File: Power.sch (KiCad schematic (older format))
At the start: 15 parts, among them U301 AOZ6605PI-1

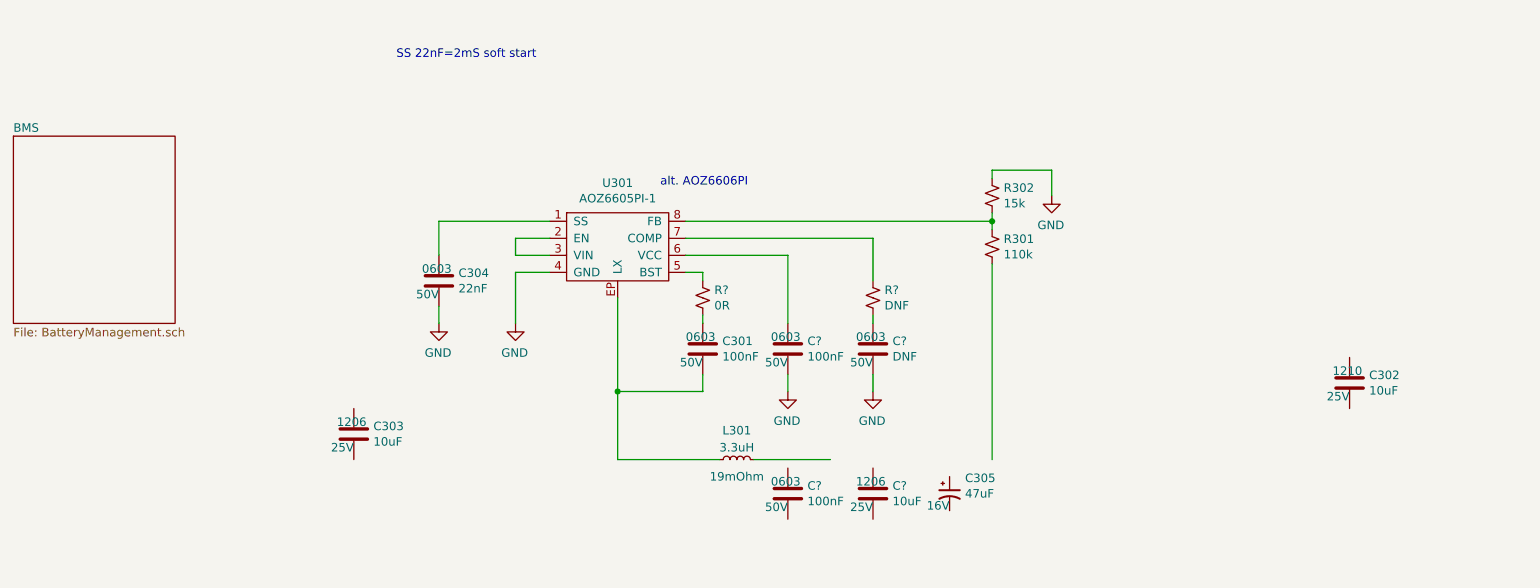
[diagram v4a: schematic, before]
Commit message: Changing structure, RM old power circuitry.
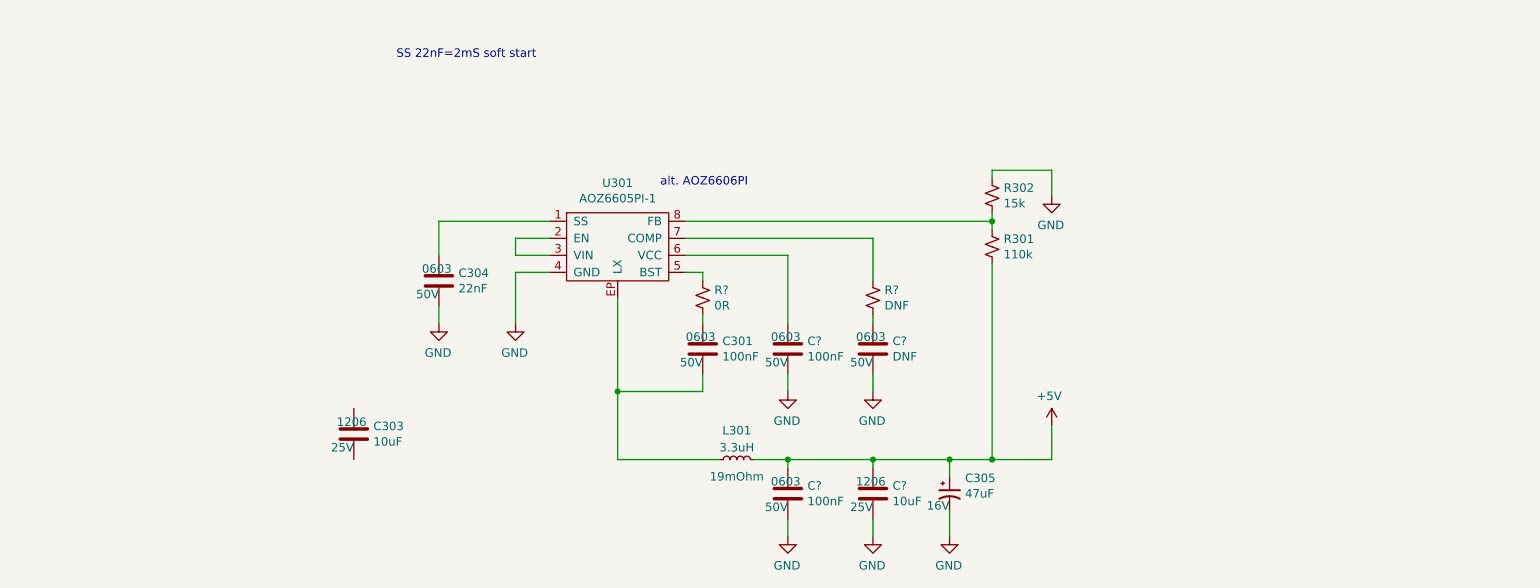
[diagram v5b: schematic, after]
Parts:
- removed C302: 10uF, Capacitors_SMD:C_1210, symbol Device:C
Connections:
- net labels added: +5V
- wire segments 31 -> 42
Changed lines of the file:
@@
 	1    0    0    -1
 $EndComp
-$Sheet
-S 1200 2350 950  1100
-U 5DAAD200
-F0 "BMS" 50
-F1 "BatteryManagement.sch" 50
-$EndSheet
 $Comp
 L Device:L_Small L301
@@
 	4750 4250 5350 4250
 Wire Wire Line
-	5550 4250 6000 4250
-Wire Wire Line
 	6950 4250 6950 3100
 Wire Wire Line
@@
 	6950 2900 6950 2850
 Connection ~ 6950 2850
-$Comp
-L Device:C C?
-U 1 1 5DB90873
-P 9050 3800
-AR Path="/5DB90873" Ref="C?"  Part="1"
-AR Path="/5DA95EB0/5DB90873" Ref="C302"  Part="1"
-F 0 "C302" H 9165 3846 50  0000 L CNN
-F 1 "10uF" H 9165 3755 50  0000 L CNN
-F 2 "Capacitors_SMD:C_1210" H 9088 3650 50  0001 C CNN
-F 3 "~" H 9050 3800 50  0001 C CNN
-F 4 "1210" H 8950 3900 50  0000 L TNN "Package"
-F 5 "Digi-Key" H 9050 3800 50  0001 C CNN "Supplier 1"
-F 6 "1276-1854-1-ND" H 9050 3800 50  0001 C CNN "Supplier Part Number 1"
-F 7 "CAP CER 10UF 25V X5R 1210" H 9050 3800 50  0001 C CNN "Description"
-F 8 "25V" H 9050 3750 50  0000 R TNN "Voltage Rating"
-F 9 "https://www.digikey.com/product-detail/en/samsung-electro-mechanics/CL32A106KAULNNE/1276-1854-1-ND/3889940" H 9050 3800 50  0001 C CNN "Link"
-F 10 "0.46000" H 9050 3800 50  0001 C CNN "Unit Cost A$"
-	1    9050 3800
-	1    0    0    -1
-$EndComp
 $Comp
 L Device:C C?
@@
 	1    0    0    -1
 $EndComp
+Wire Wire Line
+	5550 4250 5750 4250
+Wire Wire Line
+	5750 4300 5750 4250
+Connection ~ 5750 4250
+Wire Wire Line
+	5750 4250 6250 4250
+Wire Wire Line
+	6250 4300 6250 4250
+Connection ~ 6250 4250
+Wire Wire Line
+	6250 4250 6700 4250
+Wire Wire Line
+	6700 4350 6700 4250
+Connection ~ 6700 4250
+Wire Wire Line
+	6700 4250 6950 4250
+$Comp
+L power:GND #PWR?
+U 1 1 5DC1A903
+P 5750 4700
+AR Path="/5DC1A903" Ref="#PWR?"  Part="1"
+AR Path="/5DA95EB0/5DC1A903" Ref="#PWR?"  Part="1"
+F 0 "#PWR?" H 5750 4450 50  0001 C CNN
+F 1 "GND" H 5755 4527 50  0000 C CNN
+F 2 "" H 5750 4700 50  0001 C CNN
+F 3 "" H 5750 4700 50  0001 C CNN
+	1    5750 4700
+	-1   0    0    -1
+$EndComp
+$Comp
+L power:GND #PWR?
+U 1 1 5DC1AE90
+P 6250 4700
+AR Path="/5DC1AE90" Ref="#PWR?"  Part="1"
+AR Path="/5DA95EB0/5DC1AE90" Ref="#PWR?"  Part="1"
+F 0 "#PWR?" H 6250 4450 50  0001 C CNN
+F 1 "GND" H 6255 4527 50  0000 C CNN
+F 2 "" H 6250 4700 50  0001 C CNN
+F 3 "" H 6250 4700 50  0001 C CNN
+	1    6250 4700
+	-1   0    0    -1
+$EndComp
+$Comp
+L power:GND #PWR?
+U 1 1 5DC1B2B7
+P 6700 4700
+AR Path="/5DC1B2B7" Ref="#PWR?"  Part="1"
+AR Path="/5DA95EB0/5DC1B2B7" Ref="#PWR?"  Part="1"
+F 0 "#PWR?" H 6700 4450 50  0001 C CNN
+F 1 "GND" H 6705 4527 50  0000 C CNN
+F 2 "" H 6700 4700 50  0001 C CNN
+F 3 "" H 6700 4700 50  0001 C CNN
+	1    6700 4700
+	-1   0    0    -1
+$EndComp
+Wire Wire Line
+	6700 4550 6700 4700
+Wire Wire Line
+	6250 4600 6250 4700
+Wire Wire Line
+	5750 4600 5750 4700
+$Comp
+L power:+5V #PWR?
+U 1 1 5DC208D7
+P 7300 4050
+AR Path="/5DC208D7" Ref="#PWR?"  Part="1"
+AR Path="/5DA95EB0/5DC208D7" Ref="#PWR?"  Part="1"
+F 0 "#PWR?" H 7300 3900 50  0001 C CNN
+F 1 "+5V" H 7315 4223 50  0000 C CNN
+F 2 "" H 7300 4050 50  0001 C CNN
+F 3 "" H 7300 4050 50  0001 C CNN
+	1    7300 4050
+	-1   0    0    -1
+$EndComp
+Wire Wire Line
+	7300 4250 6950 4250
+Wire Wire Line
+	7300 4050 7300 4250
+Connection ~ 6950 4250
 $EndSCHEMATC

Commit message: Battery work, need to get on to connectors.
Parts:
- gave numbers to parts that had none: 6
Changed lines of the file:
@@
 	4750 3300 4750 3850
 $Comp
-L Device:R_Small_US R?
+L Device:R_Small_US R403
 U 1 1 5DBF0538
 P 5250 3300
-F 0 "R?" H 5182 3254 50  0000 R CNN
+F 0 "R403" H 5182 3254 50  0000 R CNN
 F 1 "0R" H 5182 3345 50  0000 R CNN
 F 2 "Resistors_SMD:R_0603" H 5250 3300 50  0001 C CNN
@@
 P 5750 3600
 AR Path="/5DBF81CD" Ref="C?"  Part="1"
-AR Path="/5DA95EB0/5DBF81CD" Ref="C?"  Part="1"
-F 0 "C?" H 5865 3646 50  0000 L CNN
+AR Path="/5DA95EB0/5DBF81CD" Ref="C404"  Part="1"
+F 0 "C404" H 5865 3646 50  0000 L CNN
 F 1 "100nF" H 5865 3555 50  0000 L CNN
 F 2 "Capacitors_SMD:C_0603" H 5788 3450 50  0001 C CNN
@@
 P 5750 3850
 AR Path="/5DBF9A25" Ref="#PWR?"  Part="1"
-AR Path="/5DA95EB0/5DBF9A25" Ref="#PWR?"  Part="1"
-F 0 "#PWR?" H 5750 3600 50  0001 C CNN
+AR Path="/5DA95EB0/5DBF9A25" Ref="#PWR0403"  Part="1"
+F 0 "#PWR0403" H 5750 3600 50  0001 C CNN
 F 1 "GND" H 5755 3677 50  0000 C CNN
 F 2 "" H 5750 3850 50  0001 C CNN
@@
 P 7300 2700
 AR Path="/5DBFC280" Ref="#PWR?"  Part="1"
-AR Path="/5DA95EB0/5DBFC280" Ref="#PWR?"  Part="1"
-F 0 "#PWR?" H 7300 2450 50  0001 C CNN
+AR Path="/5DA95EB0/5DBFC280" Ref="#PWR0408"  Part="1"
+F 0 "#PWR0408" H 7300 2450 50  0001 C CNN
 F 1 "GND" H 7305 2527 50  0000 C CNN
 F 2 "" H 7300 2700 50  0001 C CNN
@@
 	6950 2550 7300 2550
 $Comp
-L Device:R_Small_US R?
+L Device:R_Small_US R404
 U 1 1 5DBFDD41
 P 6250 3300
-F 0 "R?" H 6182 3254 50  0000 R CNN
+F 0 "R404" H 6182 3254 50  0000 R CNN
 F 1 "DNF" H 6182 3345 50  0000 R CNN
 F 2 "Resistors_SMD:R_0603" H 6250 3300 50  0001 C CNN
@@
 P 6250 3600
 AR Path="/5DBFE1F7" Ref="C?"  Part="1"
-AR Path="/5DA95EB0/5DBFE1F7" Ref="C?"  Part="1"
-F 0 "C?" H 6365 3646 50  0000 L CNN
+AR Path="/5DA95EB0/5DBFE1F7" Ref="C406"  Part="1"
+F 0 "C406" H 6365 3646 50  0000 L CNN
 F 1 "DNF" H 6365 3555 50  0000 L CNN
 F 2 "Capacitors_SMD:C_0603" H 6288 3450 50  0001 C CNN
@@
 P 6250 3850
 AR Path="/5DBFE935" Ref="#PWR?"  Part="1"
-AR Path="/5DA95EB0/5DBFE935" Ref="#PWR?"  Part="1"
-F 0 "#PWR?" H 6250 3600 50  0001 C CNN
+AR Path="/5DA95EB0/5DBFE935" Ref="#PWR0405"  Part="1"
+F 0 "#PWR0405" H 6250 3600 50  0001 C CNN
 F 1 "GND" H 6255 3677 50  0000 C CNN
 F 2 "" H 6250 3850 50  0001 C CNN
@@
 P 3700 3450
 AR Path="/5DC01D58" Ref="#PWR?"  Part="1"
-AR Path="/5DA95EB0/5DC01D58" Ref="#PWR?"  Part="1"
-F 0 "#PWR?" H 3700 3200 50  0001 C CNN
+AR Path="/5DA95EB0/5DC01D58" Ref="#PWR0402"  Part="1"
+F 0 "#PWR0402" H 3700 3200 50  0001 C CNN
 F 1 "GND" H 3705 3277 50  0000 C CNN
 F 2 "" H 3700 3450 50  0001 C CNN
@@
 P 5750 4450
 AR Path="/5DC061BD" Ref="C?"  Part="1"
-AR Path="/5DA95EB0/5DC061BD" Ref="C?"  Part="1"
-F 0 "C?" H 5865 4496 50  0000 L CNN
+AR Path="/5DA95EB0/5DC061BD" Ref="C405"  Part="1"
+F 0 "C405" H 5865 4496 50  0000 L CNN
 F 1 "100nF" H 5865 4405 50  0000 L CNN
 F 2 "Capacitors_SMD:C_0603" H 5788 4300 50  0001 C CNN
@@
 P 6250 4450
 AR Path="/5DC081D7" Ref="C?"  Part="1"
-AR Path="/5DA95EB0/5DC081D7" Ref="C?"  Part="1"
-F 0 "C?" H 6365 4496 50  0000 L CNN
+AR Path="/5DA95EB0/5DC081D7" Ref="C407"  Part="1"
+F 0 "C407" H 6365 4496 50  0000 L CNN
 F 1 "10uF" H 6365 4405 50  0000 L CNN
 F 2 "Capacitors_SMD:C_1206" H 6288 4300 50  0001 C CNN
@@
 P 5750 4700
 AR Path="/5DC1A903" Ref="#PWR?"  Part="1"
-AR Path="/5DA95EB0/5DC1A903" Ref="#PWR?"  Part="1"
-F 0 "#PWR?" H 5750 4450 50  0001 C CNN
+AR Path="/5DA95EB0/5DC1A903" Ref="#PWR0404"  Part="1"
+F 0 "#PWR0404" H 5750 4450 50  0001 C CNN
 F 1 "GND" H 5755 4527 50  0000 C CNN
 F 2 "" H 5750 4700 50  0001 C CNN
@@
 P 6250 4700
 AR Path="/5DC1AE90" Ref="#PWR?"  Part="1"
-AR Path="/5DA95EB0/5DC1AE90" Ref="#PWR?"  Part="1"
-F 0 "#PWR?" H 6250 4450 50  0001 C CNN
+AR Path="/5DA95EB0/5DC1AE90" Ref="#PWR0406"  Part="1"
+F 0 "#PWR0406" H 6250 4450 50  0001 C CNN
 F 1 "GND" H 6255 4527 50  0000 C CNN
 F 2 "" H 6250 4700 50  0001 C CNN
@@
 P 6700 4700
 AR Path="/5DC1B2B7" Ref="#PWR?"  Part="1"
-AR Path="/5DA95EB0/5DC1B2B7" Ref="#PWR?"  Part="1"
-F 0 "#PWR?" H 6700 4450 50  0001 C CNN
+AR Path="/5DA95EB0/5DC1B2B7" Ref="#PWR0407"  Part="1"
+F 0 "#PWR0407" H 6700 4450 50  0001 C CNN
 F 1 "GND" H 6705 4527 50  0000 C CNN
 F 2 "" H 6700 4700 50  0001 C CNN
@@
 P 7300 4050
 AR Path="/5DC208D7" Ref="#PWR?"  Part="1"
-AR Path="/5DA95EB0/5DC208D7" Ref="#PWR?"  Part="1"
-F 0 "#PWR?" H 7300 3900 50  0001 C CNN
+AR Path="/5DA95EB0/5DC208D7" Ref="#PWR0409"  Part="1"
+F 0 "#PWR0409" H 7300 3900 50  0001 C CNN
 F 1 "+5V" H 7315 4223 50  0000 C CNN
 F 2 "" H 7300 4050 50  0001 C CNN

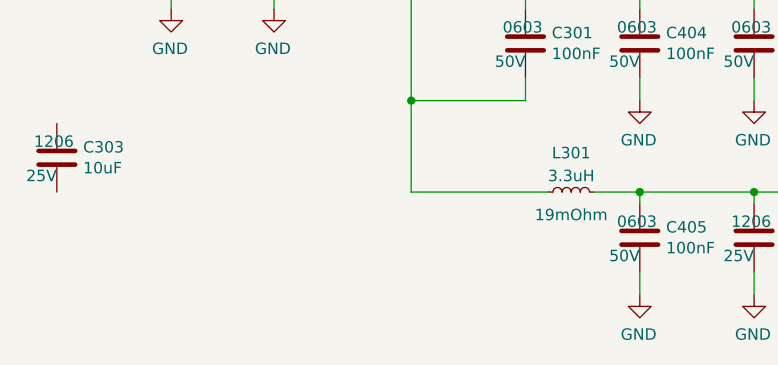
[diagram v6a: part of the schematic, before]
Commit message: Charging. Do balance next if including.
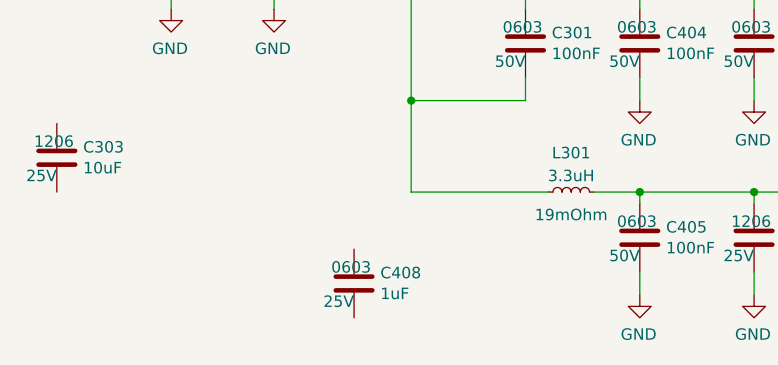
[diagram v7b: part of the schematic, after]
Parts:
- added C408: 1uF, Capacitors_SMD:C_0603, symbol Device:C
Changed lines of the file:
@@
 	7300 4050 7300 4250
 Connection ~ 6950 4250
+$Comp
+L Device:C C?
+U 1 1 5DEA1AB8
+P 4500 4650
+AR Path="/5DEA1AB8" Ref="C?"  Part="1"
+AR Path="/5DA95EB0/5DEA1AB8" Ref="C408"  Part="1"
+F 0 "C408" H 4615 4696 50  0000 L CNN
+F 1 "1uF" H 4615 4605 50  0000 L CNN
+F 2 "Capacitors_SMD:C_0603" H 4538 4500 50  0001 C CNN
+F 3 "~" H 4500 4650 50  0001 C CNN
+F 4 "0603" H 4400 4750 50  0000 L TNN "Package"
+F 5 "CAP CER 1UF 25V X5R 0603" H 4500 4650 50  0001 C CNN "Description"
+F 6 "25V" H 4500 4600 50  0000 R TNN "Voltage Rating"
+F 7 "https://www.digikey.com.au/product-detail/en/yageo/CC0603KRX5R8BB105/311-1445-1-ND/2833751" H 4500 4650 50  0001 C CNN "Link"
+F 8 "Digi-Key" H 4500 4650 50  0001 C CNN "Supplier 1"
+F 9 "311-1445-1-ND" H 4500 4650 50  0001 C CNN "Supplier Part Number 1"
+F 10 "0.15000" H 4500 4650 50  0001 C CNN "Unit Cost A$"
+	1    4500 4650
+	1    0    0    -1
+$EndComp
 $EndSCHEMATC

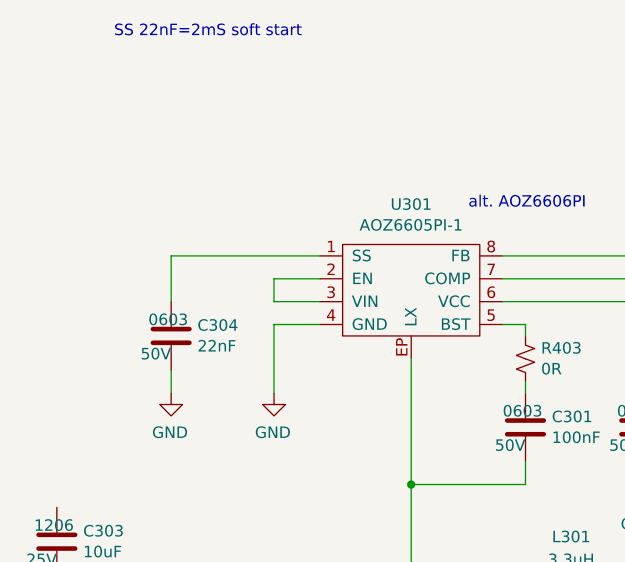
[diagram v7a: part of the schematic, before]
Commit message: Getting rid of address block on PCA9685. We don't need that many options.
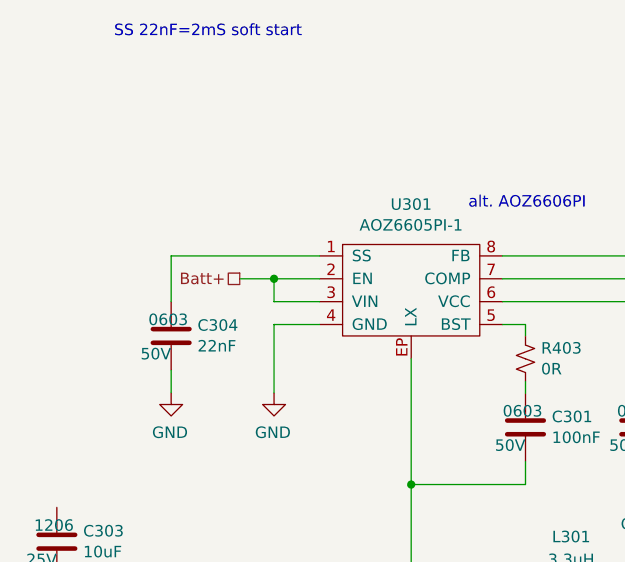
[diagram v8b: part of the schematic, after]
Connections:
- net Batt+: now reaches U301.2 (EN), U301.3 (VIN)
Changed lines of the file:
@@
 	1    0    0    -1
 $EndComp
+Text HLabel 4000 2950 0    50   UnSpc ~ 0
+Batt+
+Wire Wire Line
+	4000 2950 4150 2950
+Connection ~ 4150 2950
 $EndSCHEMATC
